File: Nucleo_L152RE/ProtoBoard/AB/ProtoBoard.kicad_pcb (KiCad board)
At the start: 2 copper layers, 68.6 x 80.5 mm, 116 parts, among them CON1 USB-MICRO-B, J1 EXT1, J2 EXT2, J3 EXTPower, P1 Power, P10 OW2_A, P11 GND1, P12 I2C1_B, P13 I2C2_B, P14 SW_1_6, P15 WS1, P16 WS2, P17 MS2, P18 WS3, P19 WS4, P2 VinPower, P20 GND2, P21 Hole, P22 MS3, P23 OW3_A, P24 OW4_A, P25 MS4, P26 Hole, P27 Hole, P28 RGB1, P29 Ant, P3 USART2, P30 Hole, P4 SWD Header, P5 USART1, P6 MS1, P7 I2C1_A, P8 I2C2_A, P9 OW1_A, Q1 SI2323DS, SW1 MomentarySwitch, U2 Nucleo-L152RE-CN7, U3 Nucleo-L152RE-CN10, U5 MT3329_GPS, U6 S25FL127S, U7 RFM69HW

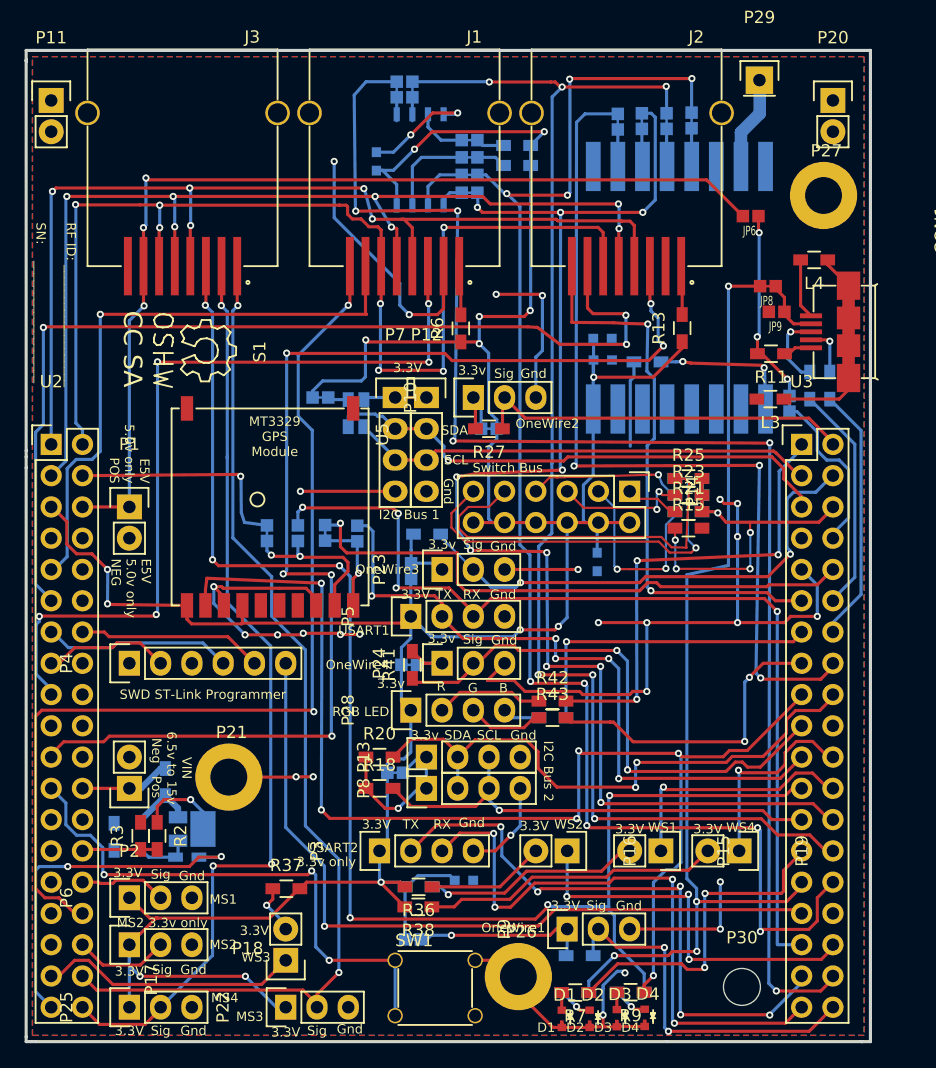
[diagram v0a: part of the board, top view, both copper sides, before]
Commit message: Making more changes on Rev AB. Found that the voltage measurement circuit didn't work as expected, so it has been replaced with a voltage divider.  Removing second Ethernet port since they take up a lot of space and the utilization of it would probably be pretty low.  Corrected many errors from Rev AA.
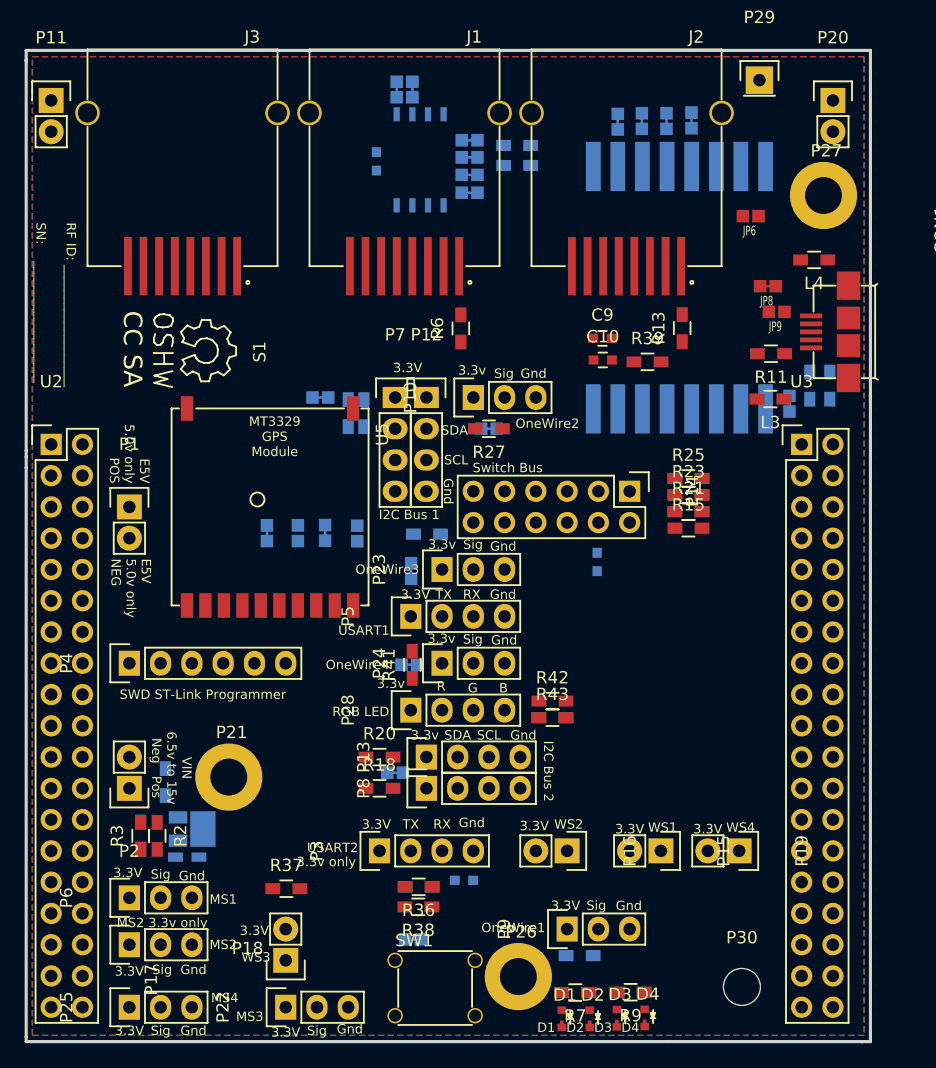
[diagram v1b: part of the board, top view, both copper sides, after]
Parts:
- C10, C9, R39: moved to F.Cu
- moved R1 2.16 mm to (131.7, 111.8)
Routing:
- net +3V3: track 265.9 -> 0.00 mm, vias 14 -> 0
- net GND: track 210.3 -> 0.00 mm, vias 29 -> 0
- net /StatusLed4: track 118.3 -> 0.00 mm, vias 6 -> 0
- net /SPI2_SCK: track 117.9 -> 0.00 mm, vias 9 -> 0
- net /FLASH_nCS: track 116.2 -> 0.00 mm, vias 5 -> 0
- net /SPI2_MOSI: track 110.5 -> 0.00 mm, vias 10 -> 0
- net /SPI2_MISO: track 108.2 -> 0.00 mm, vias 6 -> 0
- net /StatusLed3: track 98.1 -> 0.00 mm, vias 6 -> 0
- net /EXT2_SPI_CS: track 97.1 -> 0.00 mm, vias 6 -> 0
- net /EXT_SPI_MISO: track 95.1 -> 0.00 mm, vias 7 -> 0
- net /EXT_SPI_MOSI: track 85.5 -> 0.00 mm, vias 7 -> 0
- net /MotionSense3: track 84.9 -> 0.00 mm, vias 2 -> 0
- net /EXT_SPI_CLK: track 84.1 -> 0.00 mm, vias 5 -> 0
- net /E5V: track 80.9 -> 0.00 mm, vias 3 -> 0
- net /EXT1_GPIO: track 80.3 -> 0.00 mm, vias 2 -> 0
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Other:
- board text removed: "Note: 3 components under RFM module"

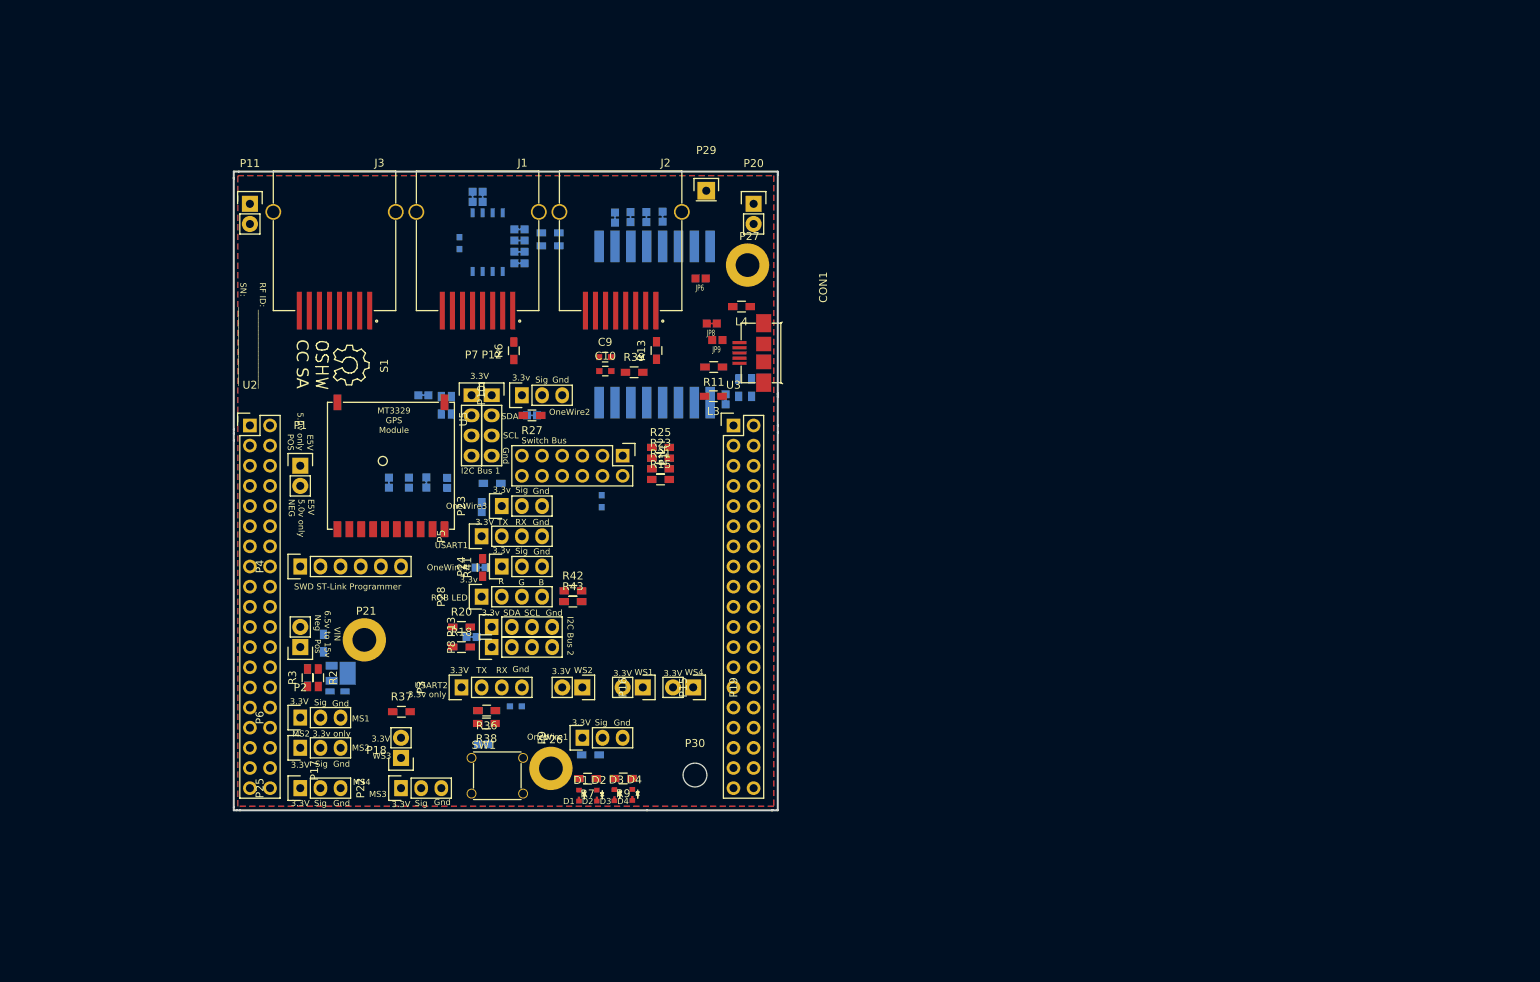
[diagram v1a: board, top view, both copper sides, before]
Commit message: Components mostly laid out into final resting positions with exception of plethora of single pin connections for easily connecting to GND, 3.3V, 5V, 3.3Vctl.
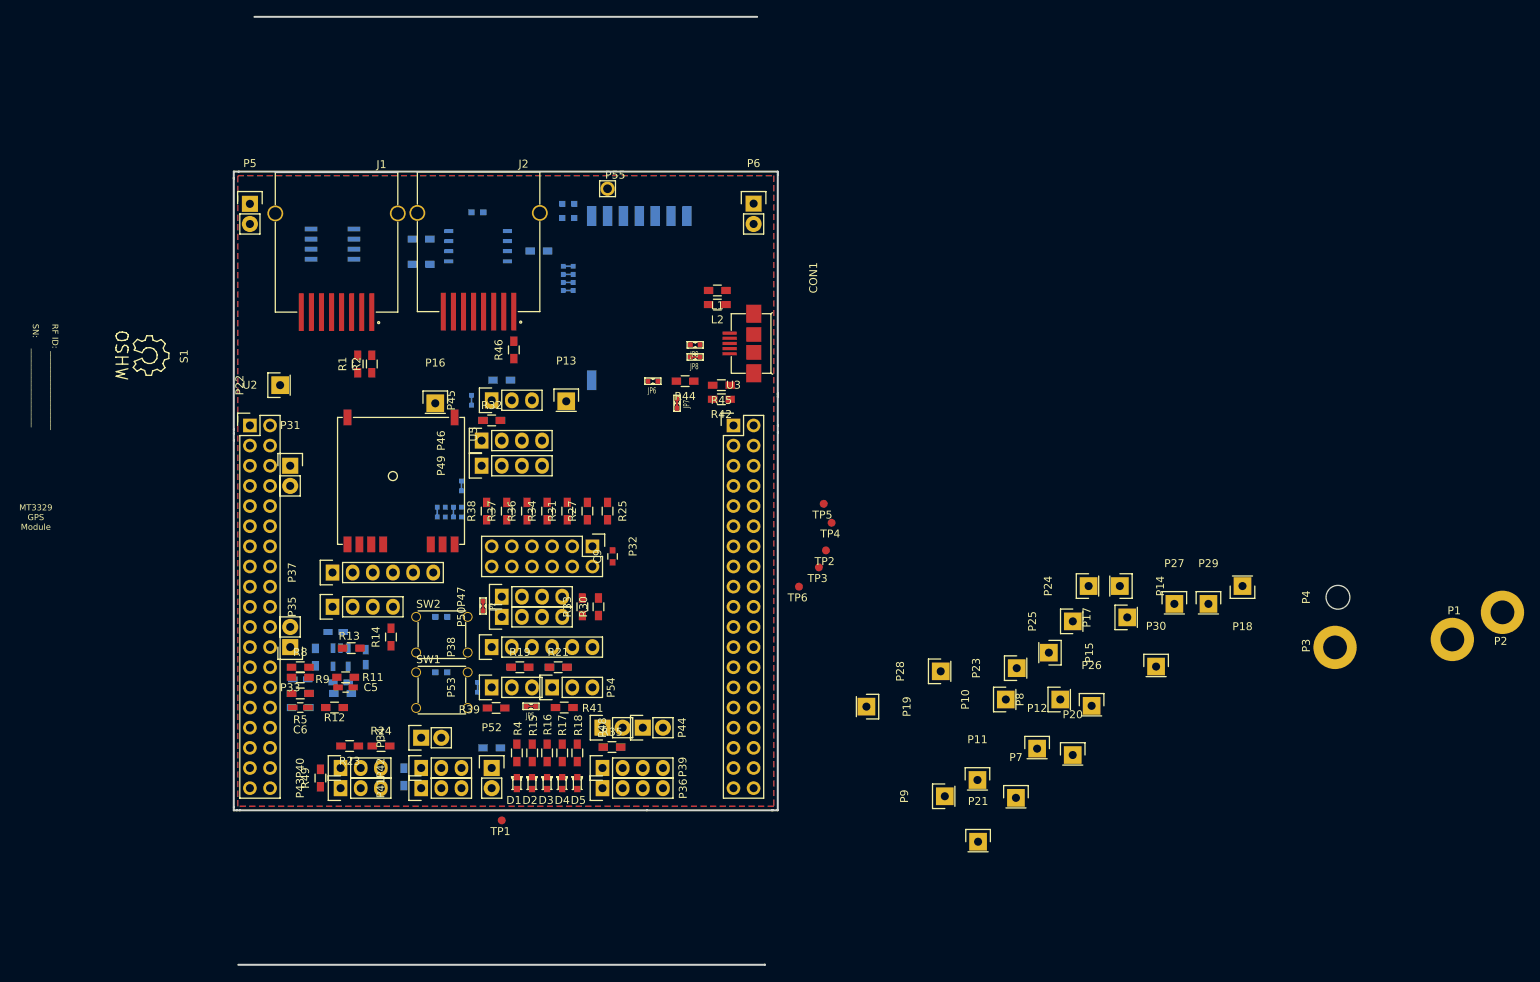
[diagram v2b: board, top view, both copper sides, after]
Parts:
- removed J3: EXTPower, nucleo:RJ45_SMD
- removed JP18, JP20, JP21, JP22, JP23, JP30, JP31, JP32, JP34, JP41, JP43, JP53, JP54, JP55, JP56, JP57, JP59: Jumper_NC_Small, nucleo:SB_NC
- removed JP19: Jumper_NO_Small, nucleo:SB_NO
- removed L3, L4: 600 Ohm, Resistors_SMD:R_0603_HandSoldering
- removed Q1: SI2323DS, nucleo:TO-236
- added C2: 10n, Capacitors_SMD:C_0603_HandSoldering, B.Cu at (139.1, 109.2)
- added C3: 1u, Capacitors_SMD:C_0603_HandSoldering, B.Cu at (135.9, 112.4)
- added C4: 0.1u, Capacitors_SMD:C_0603_HandSoldering, B.Cu at (130.8, 112.0)
- added C5: 0.1u, Capacitors_SMD:C_0603_HandSoldering, F.Cu at (136.5, 113.0)
- added C6: 0.1u, Capacitors_SMD:C_0603_HandSoldering, F.Cu at (130.8, 115.6)
- added C7: 0.1u, Capacitors_SMD:C_0603, B.Cu at (148.6, 111.1)
- added D5: Blue, nucleo:LED_0603_Standard, F.Cu at (165.7, 125.1)
- added JP1: Jumper_NC_Small, nucleo:SB_NC_Smaller, B.Cu at (151.1, 87.6)
- added JP10: Jumper_NC_Small, nucleo:SB_NC_Smaller, B.Cu at (148.1, 90.9)
- added JP11: Jumper_NO_Small, nucleo:SB_NO_Smaller, B.Cu at (149.1, 90.9)
- added JP12: Jumper_NC_Small, nucleo:SB_NC_Smaller, B.Cu at (150.1, 90.9)
- added JP13: Jumper_NO_Small, nucleo:SB_NO_Smaller, B.Cu at (151.1, 90.9)
- added JP14: Jumper_NC_Small, nucleo:SB_NC_Smaller, B.Cu at (164.6, 63.0)
- added JP15: Jumper_NC_Small, nucleo:SB_NC_Smaller, B.Cu at (164.6, 62.0)
- added JP2: Jumper_NC_Small, nucleo:SB_NC_Smaller, F.Cu at (153.8, 102.8)
- added JP3: Jumper_NC_Small, nucleo:SB_NC_Smaller, B.Cu at (152.4, 76.8)
- added JP4: Jumper_NC_Small, nucleo:SB_NC_Smaller, B.Cu at (153.2, 113.0)
- added JP5: Jumper_NC_Small, nucleo:SB_NC_Smaller, F.Cu at (159.9, 115.4)
- added L1: 600 Ohm, Resistors_SMD:R_0603_HandSoldering, F.Cu at (183.4, 63.0)
- added L2: 600 Ohm, Resistors_SMD:R_0603_HandSoldering, F.Cu at (183.4, 64.8)
- added P31: Power2, Pin_Headers:Pin_Header_Straight_1x02, F.Cu at (129.5, 85.1)
- added P32: SWBUS1, Pin_Headers:Pin_Header_Straight_2x06, F.Cu at (167.6, 95.2)
- added P33: VinPower, Pin_Headers:Pin_Header_Straight_1x02, F.Cu at (129.5, 108.0)
- added P34: ServoPower, Pin_Headers:Pin_Header_Straight_1x02, F.Cu at (146.1, 119.4)
- added P35: Power1, Pin_Headers:Pin_Header_Straight_1x04, F.Cu at (134.9, 102.9)
- added P36: USART2, Pin_Headers:Pin_Header_Straight_1x04, F.Cu at (168.9, 125.7)
- added P37: SWD Header, Pin_Headers:Pin_Header_Straight_1x06, F.Cu at (134.9, 98.6)
- added P38: RGB1, Pin_Headers:Pin_Header_Straight_1x06, F.Cu at (154.9, 108.0)
- added P39: USART1, Pin_Headers:Pin_Header_Straight_1x04, F.Cu at (168.9, 123.2)
- added P40: MS1, Pin_Headers:Pin_Header_Straight_1x03, F.Cu at (135.9, 123.2)
- added P41: MS3, Pin_Headers:Pin_Header_Straight_1x03, F.Cu at (146.1, 125.7)
- added P42: MS2, Pin_Headers:Pin_Header_Straight_1x03, F.Cu at (146.1, 123.2)
- added P43: MS4, Pin_Headers:Pin_Header_Straight_1x03, F.Cu at (135.9, 125.7)
- added P44: WS1, Pin_Headers:Pin_Header_Straight_1x02, F.Cu at (168.9, 118.1)
- added P45: OW1_A, Pin_Headers:Pin_Header_Straight_1x03, F.Cu at (154.9, 76.8)
- added P46: I2C1_A, Pin_Headers:Pin_Header_Straight_1x04, F.Cu at (153.7, 81.9)
- added P47: I2C2_A, Pin_Headers:Pin_Header_Straight_1x04, F.Cu at (156.2, 101.6)
- added P48: WS2, Pin_Headers:Pin_Header_Straight_1x02, F.Cu at (174.0, 118.1)
- added P49: I2C1_B, Pin_Headers:Pin_Header_Straight_1x04, F.Cu at (153.7, 85.1)
- added P50: I2C2_B, Pin_Headers:Pin_Header_Straight_1x04, F.Cu at (156.2, 104.1)
- added P52: WS3, Pin_Headers:Pin_Header_Straight_1x02, F.Cu at (154.9, 123.2)
- added P53: OW2_A, Pin_Headers:Pin_Header_Straight_1x03, F.Cu at (154.9, 113.0)
- added P54: OW3_A, Pin_Headers:Pin_Header_Straight_1x03, F.Cu at (162.6, 113.0)
- added P55: Ant, nucleo:Antenna_1pin, F.Cu at (169.5, 50.2)
- added R29: 2.2k, Resistors_SMD:R_0603_HandSoldering, B.Cu at (154.9, 79.4)
- added R30: 2.2k, Resistors_SMD:R_0603_HandSoldering, F.Cu at (168.4, 102.9)
- added R31: 4.7K, Resistors_SMD:R_0603_HandSoldering, F.Cu at (164.5, 90.8)
- added R32: 2.2k, Resistors_SMD:R_0603_HandSoldering, F.Cu at (154.9, 79.4)
- added R33: 2.2k, Resistors_SMD:R_0603_HandSoldering, F.Cu at (166.4, 102.9)
- added R34: 2.2K, Resistors_SMD:R_0603_HandSoldering, F.Cu at (161.9, 90.8)
- added R45: 33, Resistors_SMD:R_0603_HandSoldering, F.Cu at (183.9, 74.9)
- added R46: 0, Resistors_SMD:R_0603_HandSoldering, F.Cu at (157.7, 70.5)
- added R47: 100k, Resistors_SMD:R_0603_HandSoldering, B.Cu at (160.9, 58.0)
- added R48: 100k, Resistors_SMD:R_0603_HandSoldering, B.Cu at (146.1, 56.5)
- added R49: 0, Resistors_SMD:R_0603_HandSoldering, F.Cu at (133.3, 124.5)
- added R50: 0, Resistors_SMD:R_0603_HandSoldering, B.Cu at (143.9, 124.3)
- added SW2: ResetSwitch, nucleo:Tact_switch, F.Cu at (145.4, 104.1)
- added TP1: tp, nucleo:TestPoint_1mm, F.Cu at (156.2, 129.8)
- added TP2: tp, nucleo:TestPoint_1mm, F.Cu at (197.1, 95.8)
- added TP3: tp, nucleo:TestPoint_1mm, F.Cu at (196.2, 97.9)
- added TP4: tp, nucleo:TestPoint_1mm, F.Cu at (197.8, 92.3)
- added TP5: tp, nucleo:TestPoint_1mm, F.Cu at (196.8, 89.9)
- added TP6: tp, nucleo:TestPoint_1mm, F.Cu at (193.7, 100.3)
- added U1: LDS3985, nucleo:SOT23-5L, B.Cu at (135.9, 109.2)
- added U4: S25FL127S, nucleo:SOIC-8-FLASH, B.Cu at (153.2, 57.4)
- C1: value 0.1u -> 1u
- C10, R6: moved to B.Cu
- D1: footprint nucleo:LED_0603 -> nucleo:LED_0603_Standard
- D2: value Yellow -> Red; footprint nucleo:LED_0603 -> nucleo:LED_0603_Standard
- D3: value Green -> Yellow; footprint nucleo:LED_0603 -> nucleo:LED_0603_Standard
- D4: value Blue -> Green; footprint nucleo:LED_0603 -> nucleo:LED_0603_Standard
- J1: value EXT1 -> EXTPower
- J2: value EXT2 -> EXT
- JP16, JP8: footprint nucleo:SB_NC -> nucleo:SB_NC_Smaller
- JP17: value Jumper_NO_Small -> Jumper_NC_Small; footprint nucleo:SB_NO -> nucleo:SB_NC_Smaller
- JP6, JP9: footprint nucleo:SB_NO -> nucleo:SB_NO_Smaller
- JP7: footprint nucleo:SB_NC -> nucleo:SB_NC_Smaller; moved to F.Cu
- P1: value Power -> Hole; footprint Pin_Headers:Pin_Header_Straight_1x02 -> nucleo:plat_hole_4_20
- P10: value OW2_A -> GND; footprint Pin_Headers:Pin_Header_Straight_1x03 -> Pin_Headers:Pin_Header_Straight_1x01
- P11: value GND1 -> GND; footprint Pin_Headers:Pin_Header_Straight_1x02 -> Pin_Headers:Pin_Header_Straight_1x01
- P12: value I2C1_B -> GND; footprint Pin_Headers:Pin_Header_Straight_1x04 -> Pin_Headers:Pin_Header_Straight_1x01
- P13: value I2C2_B -> GND; footprint Pin_Headers:Pin_Header_Straight_1x04 -> Pin_Headers:Pin_Header_Straight_1x01
- P14: value SW_1_6 -> GND; footprint Pin_Headers:Pin_Header_Straight_2x06 -> Pin_Headers:Pin_Header_Straight_1x01
- P15: value WS1 -> GND; footprint Pin_Headers:Pin_Header_Straight_1x02 -> Pin_Headers:Pin_Header_Straight_1x01
- P16: value WS2 -> GND; footprint Pin_Headers:Pin_Header_Straight_1x02 -> Pin_Headers:Pin_Header_Straight_1x01
- P17: value MS2 -> GND; footprint Pin_Headers:Pin_Header_Straight_1x03 -> Pin_Headers:Pin_Header_Straight_1x01
- P18: value WS3 -> GND; footprint Pin_Headers:Pin_Header_Straight_1x02 -> Pin_Headers:Pin_Header_Straight_1x01
- P19: value WS4 -> 3.3Ctl; footprint Pin_Headers:Pin_Header_Straight_1x02 -> Pin_Headers:Pin_Header_Straight_1x01
- P2: value VinPower -> Hole; footprint Pin_Headers:Pin_Header_Straight_1x02 -> nucleo:plat_hole_4_20
- P20: value GND2 -> 3.3Ctl; footprint Pin_Headers:Pin_Header_Straight_1x02 -> Pin_Headers:Pin_Header_Straight_1x01
- P21: value Hole -> 3.3Ctl; footprint nucleo:plat_hole_4_20 -> Pin_Headers:Pin_Header_Straight_1x01
- P22: value MS3 -> 3.3V; footprint Pin_Headers:Pin_Header_Straight_1x03 -> Pin_Headers:Pin_Header_Straight_1x01
- P23: value OW3_A -> 3.3V; footprint Pin_Headers:Pin_Header_Straight_1x03 -> Pin_Headers:Pin_Header_Straight_1x01
- P24: value OW4_A -> 3.3V; footprint Pin_Headers:Pin_Header_Straight_1x03 -> Pin_Headers:Pin_Header_Straight_1x01
- P25: value MS4 -> 5.0V; footprint Pin_Headers:Pin_Header_Straight_1x03 -> Pin_Headers:Pin_Header_Straight_1x01
- P26, P27: value Hole -> 5.0V; footprint nucleo:plat_hole_4_20 -> Pin_Headers:Pin_Header_Straight_1x01
- P28: value RGB1 -> Servo; footprint Pin_Headers:Pin_Header_Straight_1x04 -> Pin_Headers:Pin_Header_Straight_1x01
- P29: value Ant -> Servo
- P3: value USART2 -> Hole; footprint Pin_Headers:Pin_Header_Straight_1x04 -> nucleo:plat_hole_4_20
- P30: value Hole -> Servo; footprint Mounting_Holes:MountingHole_3mm -> Pin_Headers:Pin_Header_Straight_1x01
- P4: value SWD Header -> Hole; footprint Pin_Headers:Pin_Header_Straight_1x06 -> Mounting_Holes:MountingHole_3mm
- P5: value USART1 -> GND1; footprint Pin_Headers:Pin_Header_Straight_1x04 -> Pin_Headers:Pin_Header_Straight_1x02
- P6: value MS1 -> GND2; footprint Pin_Headers:Pin_Header_Straight_1x03 -> Pin_Headers:Pin_Header_Straight_1x02
- P7: value I2C1_A -> GND; footprint Pin_Headers:Pin_Header_Straight_1x04 -> Pin_Headers:Pin_Header_Straight_1x01
- P8: value I2C2_A -> GND; footprint Pin_Headers:Pin_Header_Straight_1x04 -> Pin_Headers:Pin_Header_Straight_1x01
- P9: value OW1_A -> GND; footprint Pin_Headers:Pin_Header_Straight_1x03 -> Pin_Headers:Pin_Header_Straight_1x01
- R1: value 10K -> 0; moved to F.Cu
- R10: value 1k -> 976k 1%
- R11: value 0 -> 976k 1%
- R12: value 33 -> 976k 1%; moved to F.Cu
- R13: value 0 -> 332k 1%
- R14: value 100k -> 332k 1%; moved to F.Cu
- R15: value 10k -> 1K
- R16: value 100k -> 1k; moved to F.Cu
- R17: value 2.2k -> 1k; moved to F.Cu
- R18: value 2.2k -> 1k
- R19: value 2.2k -> 220; moved to F.Cu
- R2: value 2.20k 1% -> 0
- R20: value 2.2k -> 220; moved to B.Cu
- R21: value 10k -> 220
- R22: value 4.7K -> 220
- R23: value 2.2K -> 0
- R24: value 680 -> 0; moved to F.Cu
- R25: value 390 -> 10k
- R26, R40: value 4.7k -> 0
- R27: value 4.7k -> 10k
- R28: value 220 -> 4.7k
- R3: value 8.66k 1% -> 0; moved to B.Cu
- R35: moved to F.Cu
- R36: value 0 -> 680
- R37: value 0 -> 390
- R38: value 0 -> 220
- R39: value 10k -> 4.7k
- R4: value 0 -> 1K; moved to F.Cu
- R42: value 220 -> 33
- R43: value 220 -> 100k; moved to B.Cu
- R44: value 220 -> 0; moved to F.Cu
- R5: value 33 -> 0; moved to F.Cu
- R7: value 1K -> 0; moved to B.Cu
- R8: value 1k -> 0; moved to F.Cu
- R9: value 1k -> 3.6M 1%
- U5: footprint nucleo:MT3329 -> nucleo:MT3329_LessPins
- U6: value S25FL127S -> RFM69HW; footprint nucleo:SOIC-8-FLASH -> nucleo:RFM69HW_LessPins
- U7: value RFM69HW -> ATSHA204A; footprint nucleo:RFM69HW -> nucleo:8-SOIC-JEDEC_MS-012AA
- moved P2 151.6 mm to (282.4, 103.5)
- moved P1 146.9 mm to (276.0, 107.0)
- moved P4 130.9 mm to (261.6, 101.7)
- moved P11 117.0 mm to (216.2, 124.7)
- moved P3 110.3 mm to (261.3, 108.0)
- moved P18 108.3 mm to (249.6, 100.3)
- moved P17 105.5 mm to (235.1, 104.2)
- moved P25 99.6 mm to (228.2, 104.7)
- moved P6 86.4 mm to (188.0, 52.1), turned to 0 degrees
- moved P7 85.4 mm to (221.0, 127.0)
- moved P29 82.0 mm to (245.3, 102.5)
- moved P12 81.9 mm to (223.7, 120.8)
- moved P21 81.4 mm to (216.3, 132.5)
- moved P20 80.3 mm to (228.2, 121.6)
- moved P24 74.0 mm to (230.2, 100.3)
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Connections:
- net /EXT_SPI_CLK renamed EXT_SPI_SCK
- net /EXT_SPI_MISO renamed EXT_SPI_MISO
- net /EXT_SPI_MOSI renamed EXT_SPI_MOSI
- net /StatusButton1 renamed StatusButton1
- net /U5V renamed U5V
- C1 pad 1: Net-(C1-Pad1) -> GND
- C1 pad 2: /VIN_Trig -> 5V
- C8 pad 1: +3V3 -> NRST
- C9 pad 1: +3V3 -> 3.3Vctl
- D1 pad 1: Net-(D1-Pad1) -> GND
- D1 pad 2: GND -> Net-(D1-Pad2)
- D2 pad 1: Net-(D2-Pad1) -> GND
- D2 pad 2: GND -> Net-(D2-Pad2)
- D3 pad 1: Net-(D3-Pad1) -> GND
- D3 pad 2: GND -> Net-(D3-Pad2)
- D4 pad 1: Net-(D4-Pad1) -> GND
- D4 pad 2: GND -> Net-(D4-Pad2)
- J1 pad 3: /EXT1_SPI_CS -> StatusLed4
- J1 pad 7: /EXT1_ADC -> MotionSense3
- J1 pad 8: /EXT1_GPIO -> MotionSense4
- J2 pad 3: /EXT2_SPI_CS -> EXT_SPI_CS
- J2 pad 7: /EXT2_ADC -> EXT_ADC
- J2 pad 8: /EXT2_GPIO -> EXT_GPIO
- JP16 pad 1: /GPS_RX -> Net-(JP16-Pad1)
- JP16 pad 2: Net-(JP16-Pad2) -> SPI2_MISO
- JP17 pad 1: /USART1_RX -> Net-(JP17-Pad1)
- JP17 pad 2: Net-(JP16-Pad2) -> SPI2_SCK
- JP6 pad 1: /E5V -> 5V
- JP8 pad 1: /StatusLed2 -> StatusLed2
- P1 pad 1: /E5V -> GND
- P10 pad 1: Net-(JP43-Pad1) -> GND
- P12 pad 1: Net-(JP32-Pad2) -> GND
- P13 pad 1: Net-(JP34-Pad2) -> GND
- P14 pad 1: Net-(P14-Pad1) -> GND
- P15 pad 1: /WS1 -> GND
- P16 pad 1: /WS2 -> GND
- P17 pad 1: +3V3 -> GND
- P18 pad 1: /WS3 -> GND
- P19 pad 1: /WS4 -> 3.3Ctl
- P2 pad 1: +15V -> GND
- P20 pad 1: GND -> 3.3Ctl
- P21 pad 1: GND -> 3.3Ctl
- P23 pad 1: Net-(JP57-Pad1) -> +3V3
- P24 pad 1: Net-(JP59-Pad1) -> +3V3
- P25 pad 1: +3V3 -> 5V
- P26 pad 1: GND -> 5V
- P27 pad 1: GND -> 5V
- P28 pad 1: +3V3 -> ServoPower
- P29 pad 1: Net-(P29-Pad1) -> ServoPower
- P3 pad 1: +3V3 -> GND
- P30 pad 1: (no net) -> ServoPower
- P5 pad 1: +3V3 -> GND
- P5 pad 2: /USART1_TX -> GND
- P6 pad 1: +3V3 -> GND
- P6 pad 2: /MotionSense1 -> GND
- P7 pad 1: Net-(JP32-Pad2) -> GND
- P8 pad 1: Net-(JP34-Pad2) -> GND
- P9 pad 1: Net-(JP41-Pad1) -> GND
- R1 pad 1: Net-(Q1-Pad2) -> 5V
- R1 pad 2: Net-(C1-Pad1) -> Net-(J1-Pad1)
- R10 pad 1: /StatusLed4 -> Net-(C4-Pad2)
- R10 pad 2: Net-(D4-Pad1) -> GND
- R11 pad 1: Net-(CON1-Pad1) -> Net-(C5-Pad2)
- R11 pad 2: Net-(JP6-Pad2) -> GND
- R12 pad 1: /USB_DM -> Net-(C6-Pad2)
- R12 pad 2: Net-(CON1-Pad2) -> GND
- R13 pad 1: +3V3 -> Net-(P35-Pad3)
- R13 pad 2: Net-(J2-Pad1) -> Net-(C5-Pad2)
- R14 pad 1: Net-(JP30-Pad2) -> Net-(C6-Pad2)
- R14 pad 2: +3V3 -> Net-(P35-Pad4)
- R15 pad 1: /SWBus -> StatusLed1
- R15 pad 2: GND -> Net-(D2-Pad2)
- R16 pad 1: Net-(JP31-Pad2) -> StatusLed2
- R16 pad 2: +3V3 -> Net-(D3-Pad2)
- R17 pad 1: Net-(JP32-Pad2) -> StatusLed3
- R17 pad 2: /I2C_SCL1 -> Net-(D4-Pad2)
- R18 pad 1: Net-(JP34-Pad2) -> StatusLed4
- R18 pad 2: /I2C_SCL2 -> Net-(D5-Pad2)
- R19 pad 1: Net-(JP32-Pad2) -> Net-(P38-Pad2)
- R19 pad 2: /I2C_SDA1 -> RGB_Red
- R2 pad 1: Net-(Q1-Pad3) -> +3V3
- R2 pad 2: /VIN_Meas -> Net-(J1-Pad1)
- R20 pad 1: Net-(JP34-Pad2) -> Net-(P38-Pad3)
- R20 pad 2: /I2C_SDA2 -> RGB_Blue
- R21 pad 1: Net-(P14-Pad1) -> Net-(P38-Pad4)
- R21 pad 2: /SWBus -> RGB_Green
- R22 pad 1: Net-(P14-Pad3) -> Net-(P38-Pad5)
- R22 pad 2: /SWBus -> RGB_CS
- R23 pad 1: Net-(P14-Pad5) -> ServoPower
- R23 pad 2: /SWBus -> Net-(P40-Pad1)
- R24 pad 1: Net-(P14-Pad7) -> ServoPower
- R24 pad 2: /SWBus -> Net-(P42-Pad1)
- R25 pad 1: Net-(P14-Pad9) -> SWBus
- R25 pad 2: /SWBus -> GND
- R26 pad 1: /OneWireBus1 -> 3.3Vctl
- R26 pad 2: Net-(JP41-Pad1) -> WS1
- R27 pad 1: /OneWireBus2 -> Net-(P32-Pad1)
- R27 pad 2: Net-(JP43-Pad1) -> SWBus
- R28 pad 1: Net-(P14-Pad11) -> OneWireBus1
- R28 pad 2: /SWBus -> Net-(JP3-Pad2)
- R3 pad 1: /VIN_Meas -> +3V3
- R3 pad 2: GND -> 3.3Ctl
- R35 pad 1: Net-(P15-Pad2) -> 3.3Vctl
- R35 pad 2: +3V3 -> WS2
- R36 pad 1: Net-(P16-Pad2) -> Net-(P32-Pad7)
- R36 pad 2: +3V3 -> SWBus
- R37 pad 1: Net-(P18-Pad2) -> Net-(P32-Pad9)
- R37 pad 2: +3V3 -> SWBus
- R38 pad 1: Net-(P19-Pad2) -> Net-(P32-Pad11)
- R38 pad 2: +3V3 -> SWBus
- R39 pad 1: GND -> OneWireBus2
- R39 pad 2: Net-(R39-Pad2) -> Net-(JP4-Pad2)
- R4 pad 1: Net-(Q1-Pad2) -> Net-(D1-Pad2)
- R4 pad 2: +15V -> 3.3Ctl
- R40 pad 1: /OneWireBus3 -> 3.3Vctl
- R40 pad 2: Net-(JP57-Pad1) -> WS3
- R41 pad 1: /OneWireBus4 -> OneWireBus3
- R41 pad 2: Net-(JP59-Pad1) -> Net-(JP5-Pad2)
- R42 pad 1: Net-(P28-Pad2) -> USB_DP
- R42 pad 2: /RGB_Red -> Net-(CON1-Pad3)
- R43 pad 1: Net-(P28-Pad3) -> FLASH_nCS
- R43 pad 2: /RGB_Blue -> +3V3
- R44 pad 1: Net-(P28-Pad4) -> Net-(CON1-Pad1)
- R44 pad 2: /RGB_Green -> Net-(JP6-Pad2)
- R5 pad 1: /USB_DP -> Net-(C5-Pad2)
- R5 pad 2: Net-(CON1-Pad3) -> VIN_Meas1
- R6 pad 1: +3V3 -> Net-(C6-Pad2)
- R6 pad 2: Net-(J1-Pad1) -> VIN_Meas2
- R7 pad 1: /StatusLed1 -> Net-(C4-Pad2)
- R7 pad 2: Net-(D1-Pad1) -> VIN_Meas1
- R8 pad 1: /StatusLed2 -> +15V
- R8 pad 2: Net-(D2-Pad1) -> Net-(R8-Pad2)
- R9 pad 1: /StatusLed3 -> Net-(R8-Pad2)
- R9 pad 2: Net-(D3-Pad1) -> Net-(C4-Pad2)
- U2 pad 11: /EXT2_ADC -> (no net)
- U2 pad 13: /TMS -> TMS
- U2 pad 14: /NRST -> NRST
- U2 pad 15: /TCK -> TCK
- U2 pad 17: /EXT1_SPI_CS -> EXT_GPIO
- U2 pad 18: (no net) -> 5V
- U2 pad 21: /EXT2_SPI_CS -> MotionSense1
- U2 pad 28: /VIN_Meas -> VIN_Meas1
- U2 pad 30: /MotionSense1 -> VIN_Meas2
- U2 pad 32: /EXT1_GPIO -> EXT_ADC
- U2 pad 34: /MotionSense2 -> MotionSense2
- U2 pad 35: /WS3 -> WS3
- U2 pad 36: /MotionSense3 -> MotionSense3
- U2 pad 37: /VIN_Trig -> SensorVEnable
- U2 pad 38: /MotionSense4 -> MotionSense4
- U2 pad 4: /GPS_RX -> EXT_SPI_CS
- U2 pad 6: /E5V -> E5V
- U2 pad 9: /EXT1_ADC -> (no net)
- U3 pad 1: /RGB_Red -> RGB_CS
- U3 pad 10: /GPS_TX -> (no net)
- U3 pad 11: /EXT2_GPIO -> RGB_Red
- U3 pad 12: /USB_DP -> USB_DP
- U3 pad 13: /RGB_Green -> RGB_Green
- U3 pad 14: /USB_DM -> USB_DM
- U3 pad 15: /RGB_Blue -> RGB_Blue
- U3 pad 16: /SPI2_NSS -> SPI2_NSS
- U3 pad 17: /StatusLed3 -> StatusLed3
- U3 pad 18: /I2C_SDA2 -> I2C_SDA2
- U3 pad 19: /OneWireBus4 -> OneWireBus3
- U3 pad 2: /OneWireBus2 -> FLASH_nCS
- U3 pad 21: /USART1_TX -> USART1_TX
- U3 pad 22: /WS4 -> OneWireBus2
- U3 pad 23: /StatusLed4 -> StatusLed4
- U3 pad 24: /WS1 -> WS1
- U3 pad 25: /I2C_SCL2 -> I2C_SCL2
- U3 pad 26: /SPI2_MOSI -> SPI2_MOSI
- U3 pad 27: /StatusLed1 -> StatusLed1
- U3 pad 28: /SPI2_MISO -> SPI2_MISO
- U3 pad 29: /StatusLed2 -> StatusLed2
- U3 pad 3: /I2C_SCL1 -> I2C_SCL1
- U3 pad 30: /SPI2_SCK -> SPI2_SCK
- U3 pad 31: /SWO -> SWO
- U3 pad 33: /USART1_RX -> USART1_RX
- U3 pad 34: /WS2 -> WS2
- U3 pad 35: /USART2_TX -> USART2_TX
- U3 pad 36: /FLASH_nCS -> (no net)
- U3 pad 37: /USART2_RX -> USART2_RX
- U3 pad 38: /OneWireBus1 -> (no net)
- U3 pad 4: /OneWireBus3 -> OneWireBus1
- U3 pad 5: /I2C_SDA1 -> I2C_SDA1
- U3 pad 6: /SWBus -> SWBus
- U5 pad 2: /StatusLed3 -> StatusLed3
- U5 pad 9: Net-(JP16-Pad2) -> Net-(JP10-Pad2)
- U7 pad 1: Net-(R39-Pad2) -> (no net)
- U7 pad 4: (no net) -> GND
- U7 pad 5: (no net) -> I2C_SDA1
- U7 pad 6: (no net) -> I2C_SCL1
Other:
- board size 68.6 x 80.5 mm -> 68.6 x 119.5 mm
- board text removed: "3.3V"
- board text removed: "3.3v"
- board text removed: "3.3v only"
- board text removed: "B"
- board text removed: "CC SA"
- board text removed: "D1"
- board text removed: "D2"
- board text removed: "D3"
- board text removed: "D4"
- board text removed: "E5V 5.0v only NEG"
- board text removed: "E5V 5.0v only POS"
- board text removed: "Extension 2"
- board text removed: "G"
- board text removed: "Gnd"
- board text removed: "I2C Bus 1"
- board text removed: "I2C Bus 2"
- board text removed: "MS1"
- board text removed: "MS2"
- board text removed: "MS2 3.3v only"
- board text removed: "MS3"
- board text removed: "MS4"
- board text removed: "OneWire1"
- board text removed: "OneWire2"
- board text removed: "OneWire3"
- board text removed: "OneWire4"
- board text removed: "R"
- board text removed: "RGB LED"
- board text removed: "RX"
- board text removed: "SCL"
- board text removed: "SDA"
- board text removed: "SWD ST-Link Programmer"
- board text removed: "Sig"
- board text removed: "Switch Bus"
- board text removed: "TX"
- board text removed: "USART1"
- board text removed: "USART2"
- board text removed: "VIN 6.5v to 15v Neg Pos"
- board text removed: "WS1"
- board text removed: "WS2"
- board text removed: "WS3"
- board text removed: "WS4"
